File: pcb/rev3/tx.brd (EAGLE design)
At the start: 28 x 36.5 mm, 54 parts, among them U3 MCP73831T-2ACI/OT, Y1 CRYSTAL-26MHZSMD-3.2X2.5

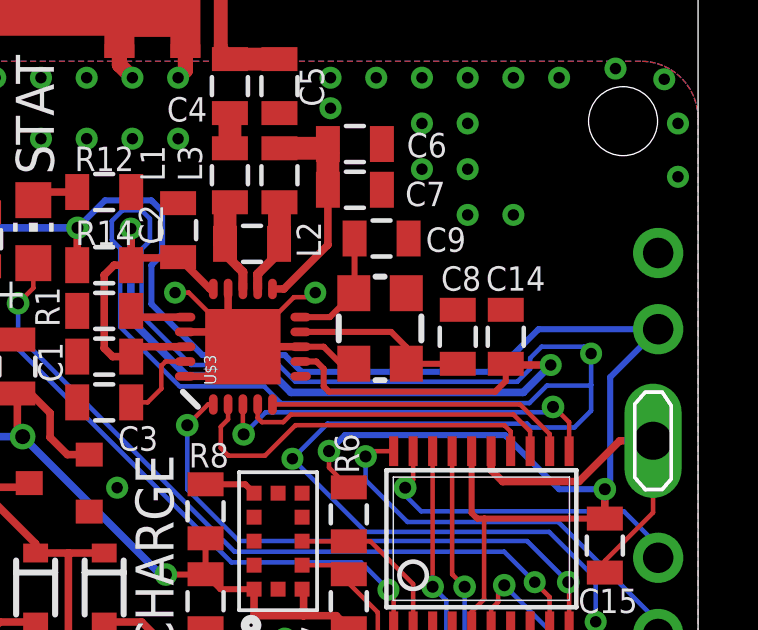
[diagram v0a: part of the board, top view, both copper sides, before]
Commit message: tx added mosfet switch
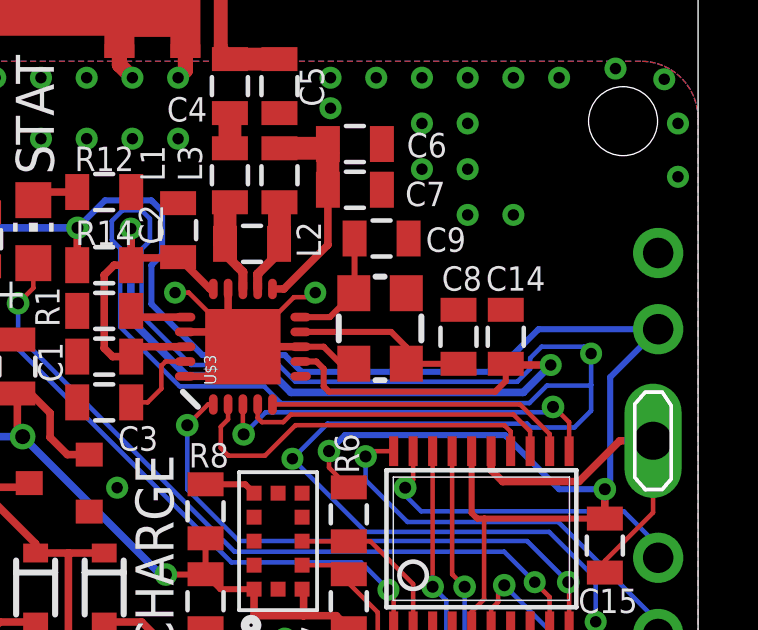
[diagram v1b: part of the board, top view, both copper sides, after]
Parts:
- C1, C14: value 100nF -> 4.7uF
- C2: value 2.2nF -> 4.7uF
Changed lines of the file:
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@@
 <attribute name="NAME" x="11.938" y="18.2118" size="0.4064" layer="25" rot="R90"/>
 </element>
-<element name="C1" library="clock" package="0805" value="100nF" x="8.2042" y="19.1516" smashed="yes" rot="R180">
+<element name="C1" library="clock" package="0805" value="4.7uF" x="8.2042" y="19.1516" smashed="yes" rot="R180">
 <attribute name="NAME" x="6.0071" y="19.6342" size="0.8128" layer="25" rot="R270"/>
 </element>
@@
 <attribute name="NAME" x="6.7183" y="20.1422" size="0.8128" layer="25" rot="R90"/>
 </element>
-<element name="C2" library="clock" package="0805" value="2.2nF" x="10.668" y="23.368" smashed="yes" rot="R90">
+<element name="C2" library="clock" package="0805" value="4.7uF" x="10.668" y="23.368" smashed="yes" rot="R90">
 <attribute name="NAME" x="10.1727" y="22.8854" size="0.8128" layer="25" rot="R90"/>
 </element>
@@
 <attribute name="NAME" x="18.2372" y="24.1681" size="0.8128" layer="25"/>
 </element>
-<element name="C8" library="clock" package="0805" value="22pF" x="19.9898" y="19.812" smashed="yes" rot="R90">
-<attribute name="NAME" x="19.431" y="21.3487" size="0.8128" layer="25"/>
+<element name="C8" library="clock" package="0805" value="22pF" x="20.0152" y="19.812" smashed="yes" rot="R90">
+<attribute name="NAME" x="19.4564" y="21.3487" size="0.8128" layer="25"/>
 </element>
 <element name="C9" library="clock" package="0805" value="22pF" x="17.4498" y="23.0886" smashed="yes">
@@
 <attribute name="NAME" x="11.303" y="8.7503" size="0.8128" layer="25"/>
 </element>
-<element name="C14" library="clock" package="0805" value="100nF" x="21.59" y="19.812" smashed="yes" rot="R90">
+<element name="C14" library="clock" package="0805" value="4.7uF" x="21.59" y="19.812" smashed="yes" rot="R90">
 <attribute name="NAME" x="20.9296" y="21.3487" size="0.8128" layer="25"/>
 </element>
@@
 <wire x1="18.274" y1="19.4704" x2="18.274" y2="18.9164" width="0.2032" layer="1"/>
 <wire x1="17.7695" y1="19.9749" x2="18.274" y2="19.4704" width="0.2032" layer="1"/>
-<wire x1="19.9898" y1="18.912" x2="18.2784" y2="18.912" width="0.2032" layer="1"/>
+<wire x1="20.0152" y1="18.912" x2="18.2784" y2="18.912" width="0.2032" layer="1"/>
 <wire x1="18.2784" y1="18.912" x2="18.274" y2="18.9164" width="0.2032" layer="1"/>
 </signal>
